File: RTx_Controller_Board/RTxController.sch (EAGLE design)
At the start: 214 parts, among them IC1 LTC4263, IC2 TLK110", SW1 COM08720, U1 STM32F407ZXT, U2 TPD4S012, X4 MINI-USB-32005-301, X8 0826-1X1T-GJ-F

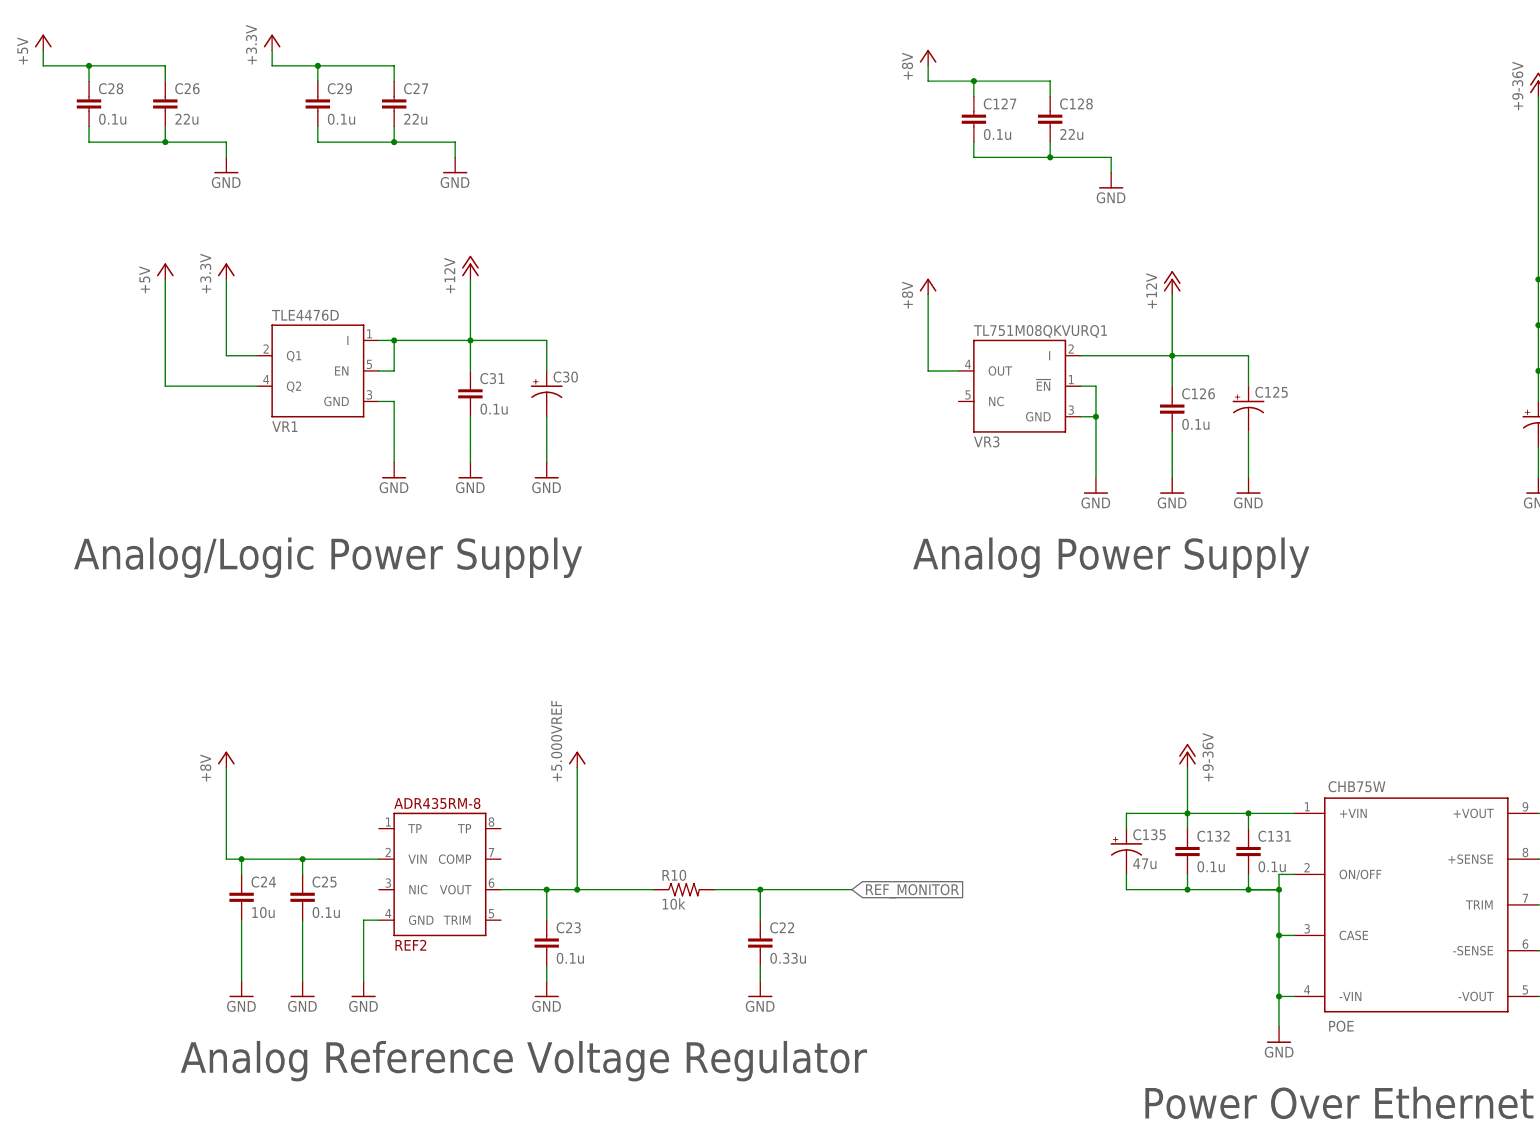
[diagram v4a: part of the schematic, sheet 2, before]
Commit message: Made modifications to address issues recorded and closed.
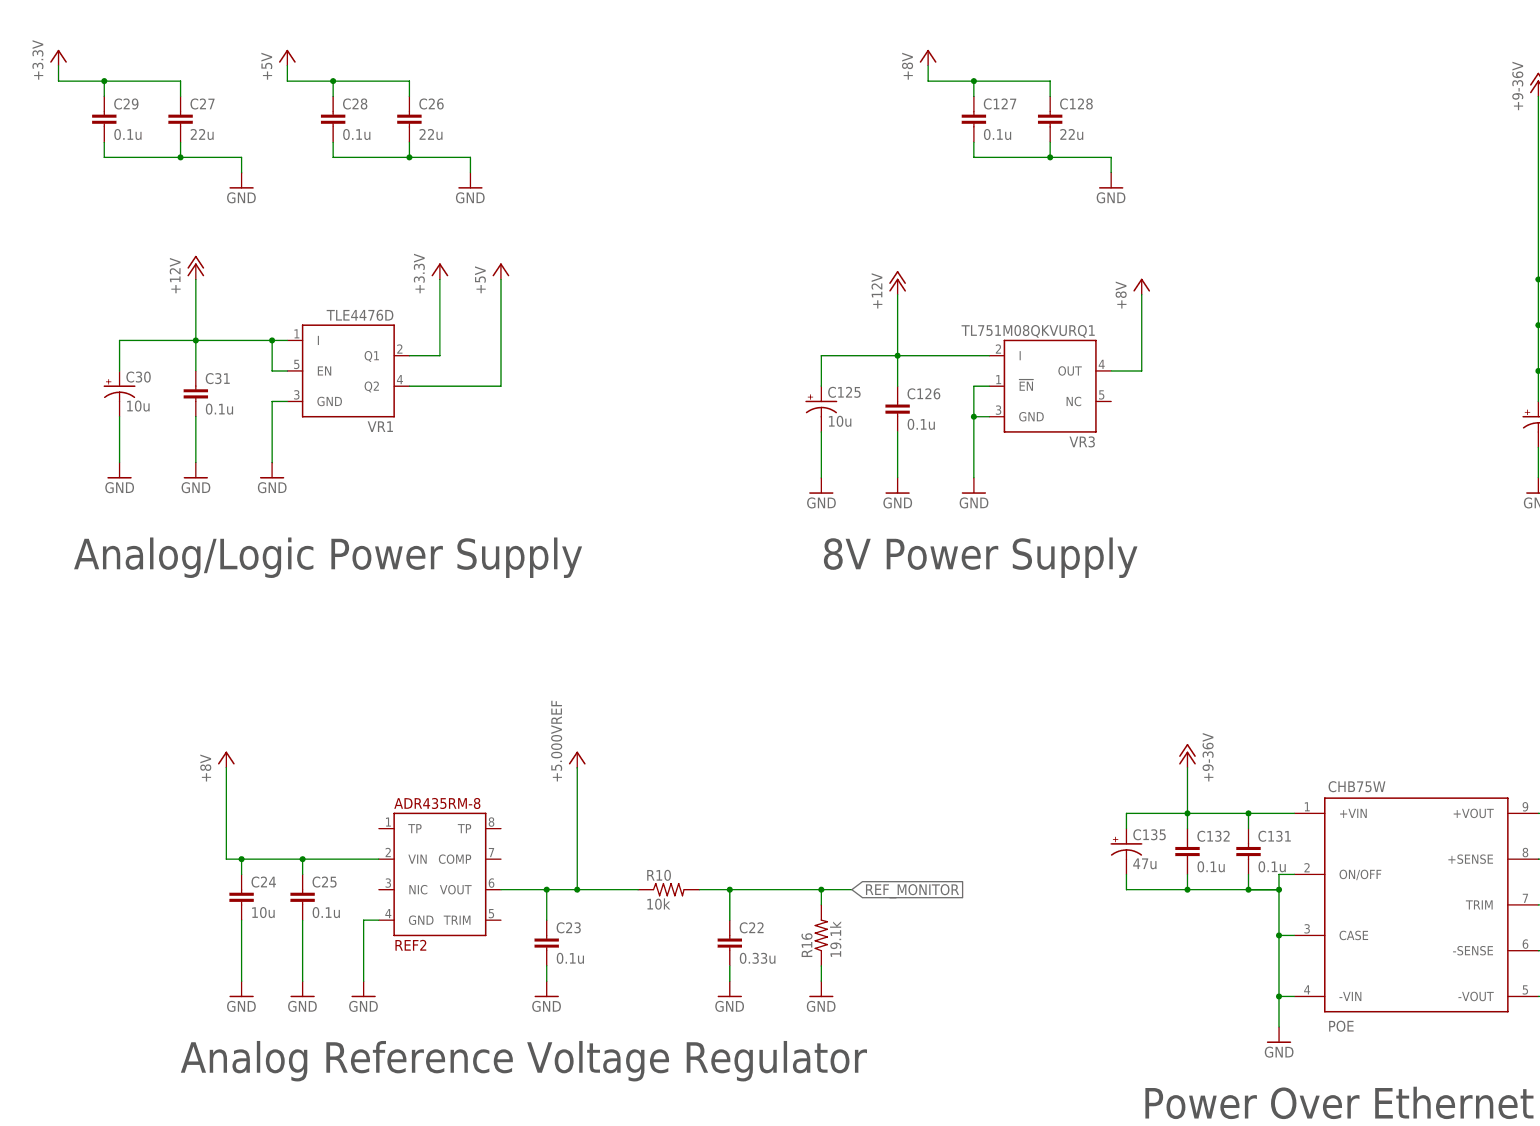
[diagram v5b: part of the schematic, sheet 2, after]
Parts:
- removed JP2: (no value), pinhead:PINHD-1X6
- removed R55, R56, R57, R58: 22, motorFeedback:R-US_R0603
- removed R59: 10k, motorFeedback:R-US_R0603
- added C55: 1u, motorFeedback:C-EUC0805
- added C72: 22u, motorFeedback:C-EUC1206
- added J22: Debug Header, headers:1.27MM_HDR_2X5
- added R16: 19.1k, motorFeedback:R-US_R0402
- added R168: 100, rcl_custom:R-US_0402-B-NOSILK
- added TP38: TPTP06R, testpad:TPTP06R
- C125, C30: value (none) -> 10u
- C92: value 0.1u -> NU
- X1: device con-subd:F09HS -> con-subd:F15HDHS
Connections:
- removed net N$30: C53.1, R23.1, R24.2
- removed net SPI_MOSI: ADC1.CNV@6, ADC1.SDI@9, ADC2.CNV@6, ADC3.CNV@6, ADC4.CNV@6, U1-IO.PB5/SPI1_MOSI@91
- removed net STM_SWCLK: R57.1, U1-IO.PA14/JTCK@76
- removed net STM_SWDIO: R56.1, U1-IO.PA13/JTMS@72
- removed net STM_SWO: R58.1, U1-IO.PB3/JTDO@89
- removed net SWD_GND1: JP2.1, R59.2
- removed net SWD_NRST: JP2.5, R55.2
- removed net SWD_SWCLK: JP2.2, R57.2
- removed net SWD_SWDIO: JP2.4, R56.2
- removed net SWD_SWO: JP2.6, R58.2
- removed net V+@8: OPAMP2-A.V+@8
- removed net VDDA: C88.1, C89.1, C90.1, C91.1, U1-PWR.VDDA@22, U1-PWR.VREF+@21
- new net ADC_CNV: U1-IO.PA4/SPI_NSS@29
- new net JTAG_TCK: J22.TCK
- new net JTAG_TDI: J22.TDI
- new net JTAG_TDO: J22.TDO
- new net JTAG_TMS: J22.TMS
- new net N$206: J22.VTREF, R168.1
- new net N$210: J22.GNDDET, TP38.TP
- new net SPI_NSS: ADC1.CNV@6, ADC1.SDI@9, ADC2.CNV@6, ADC3.CNV@6, ADC4.CNV@6
- net +3.3V: now also C53.1, C88.1, C89.1, C90.1, C91.1, R168.2, R23.1, R24.2, U1-PWR.VDDA@22, U1-PWR.VREF+@21
- net +5.000VREF: now also C55.1, C72.1, X1-12.F, X1-14.F, X1-2.F, X1-3.F; no longer X1-9.F
- net +5V: now also OPAMP2-A.V+@8
- net GND: now also C55.2, C72.2, J22.GND, J22.GND@2, R16.1, X1-5.F, X1-7.F; no longer JP2.3, R59.1, X1-2.F, X1-4.F
- net N$14: now also X1-4.F; no longer X1-3.F
- net N$6: now also X1-15.F; no longer X1-7.F
- net N$9: now also X1-11.F; no longer X1-5.F
- net NRST: now also J22.!RESET; no longer R55.1
- net REF_MONITOR: now also R16.2
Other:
- note added: "8V Power Supply"
- note added: "ADC Interrupt In"
- note added: "Debug Header"
- note added: "Ground at OpAmp"
- note added: "Place at REF pin"
- note removed: "Analog Power Supply"
- note removed: "SWD"
- moved on the sheet: C125, C126, C22, C26, C27, C28, C29, C30, C31, C44, C48, C50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

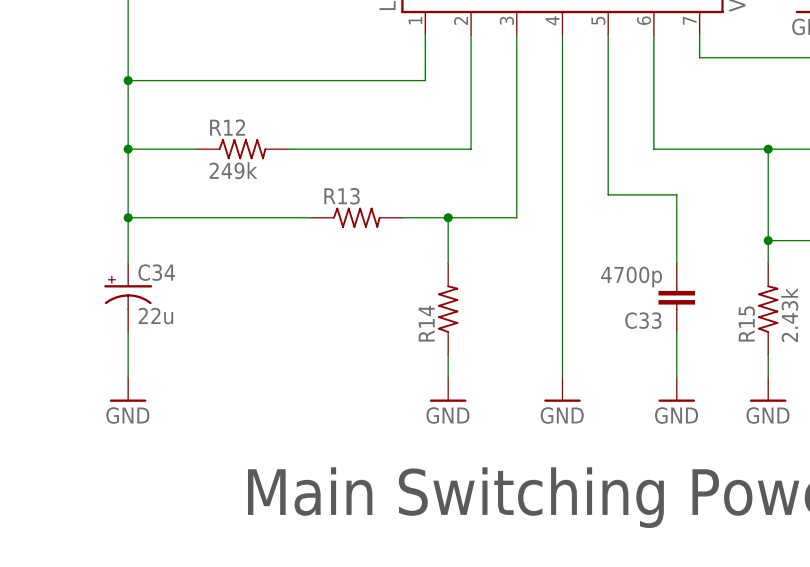
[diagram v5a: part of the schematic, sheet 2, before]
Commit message: Closed issues related to Power page of schematic.
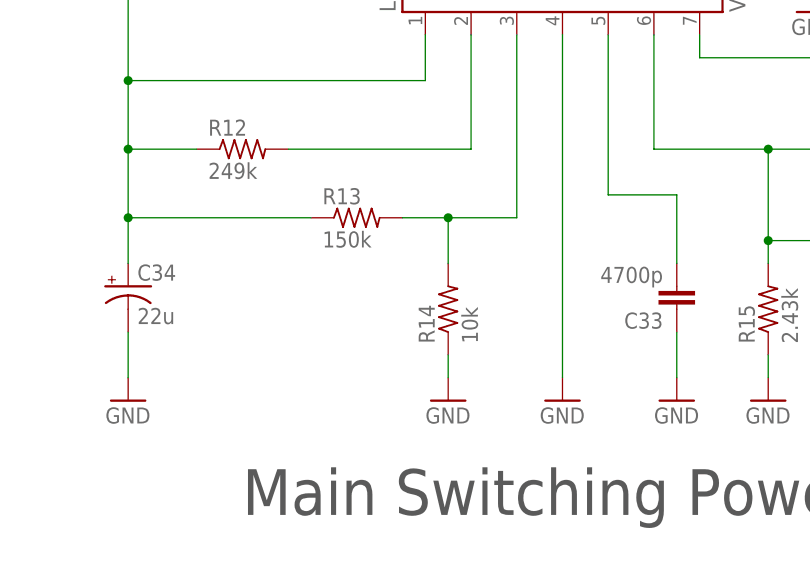
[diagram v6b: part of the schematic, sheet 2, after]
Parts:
- R13: value (none) -> 150k
- R14: value (none) -> 10k
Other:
- note added: "Add 8mil spark gaps to each signal near connector"
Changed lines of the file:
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@@
 <part name="P+19" library="motorFeedback" deviceset="+12V" device=""/>
 <part name="R12" library="motorFeedback" deviceset="R-US_" device="R0603" value="249k"/>
-<part name="R13" library="motorFeedback" deviceset="R-US_" device="R0603"/>
-<part name="R14" library="motorFeedback" deviceset="R-US_" device="R0603"/>
+<part name="R13" library="motorFeedback" deviceset="R-US_" device="R0603" value="150k"/>
+<part name="R14" library="motorFeedback" deviceset="R-US_" device="R0603" value="10k"/>
 <part name="R15" library="motorFeedback" deviceset="R-US_" device="R0603" value="2.43k"/>
 <part name="C32" library="motorFeedback" deviceset="C-EU" device="C0402" value="0.022u"/>
@@
 <text x="187.706" y="110.998" size="1.27" layer="97" rot="R180">Place at REF pin</text>
 <text x="187.706" y="52.578" size="1.27" layer="97" rot="R180">Place at REF pin</text>
+<text x="10.16" y="137.16" size="1.27" layer="97" rot="R90">Add 8mil spark gaps to each signal near connector</text>
 </plain>
 <instances>
@@
 <wire x1="398.78" y1="76.2" x2="398.78" y2="129.54" width="0.1524" layer="97" style="shortdash"/>
 <wire x1="398.78" y1="129.54" x2="332.74" y2="129.54" width="0.1524" layer="97" style="shortdash"/>
+<text x="10.16" y="25.4" size="1.27" layer="97" rot="R90">Add 8mil spark gaps to each signal near connector</text>
+<text x="10.16" y="83.82" size="1.27" layer="97" rot="R90">Add 8mil spark gaps to each signal near connector</text>
 </plain>
 <instances>

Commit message: Cleaned up schematic, began layout of RTx Controller PCB.
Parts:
- removed REF2: ADR435RM-8, motorFeedback:ADR435RM-8
- added REF1: ADR435RM-8, motorFeedback:ADR435RM-8
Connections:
- net +5.000VREF: now also REF1.VOUT@6; no longer REF2.VOUT@6
- net +8V: now also REF1.VIN@2; no longer REF2.VIN@2
- net GND: now also REF1.GND@4; no longer REF2.GND@4
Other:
- note added: "Ref Voltage Monitor Filter"
- moved on the sheet: C129, C130, C131, C132, C133, C135, C22, C23, C24, C25, C32, C33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

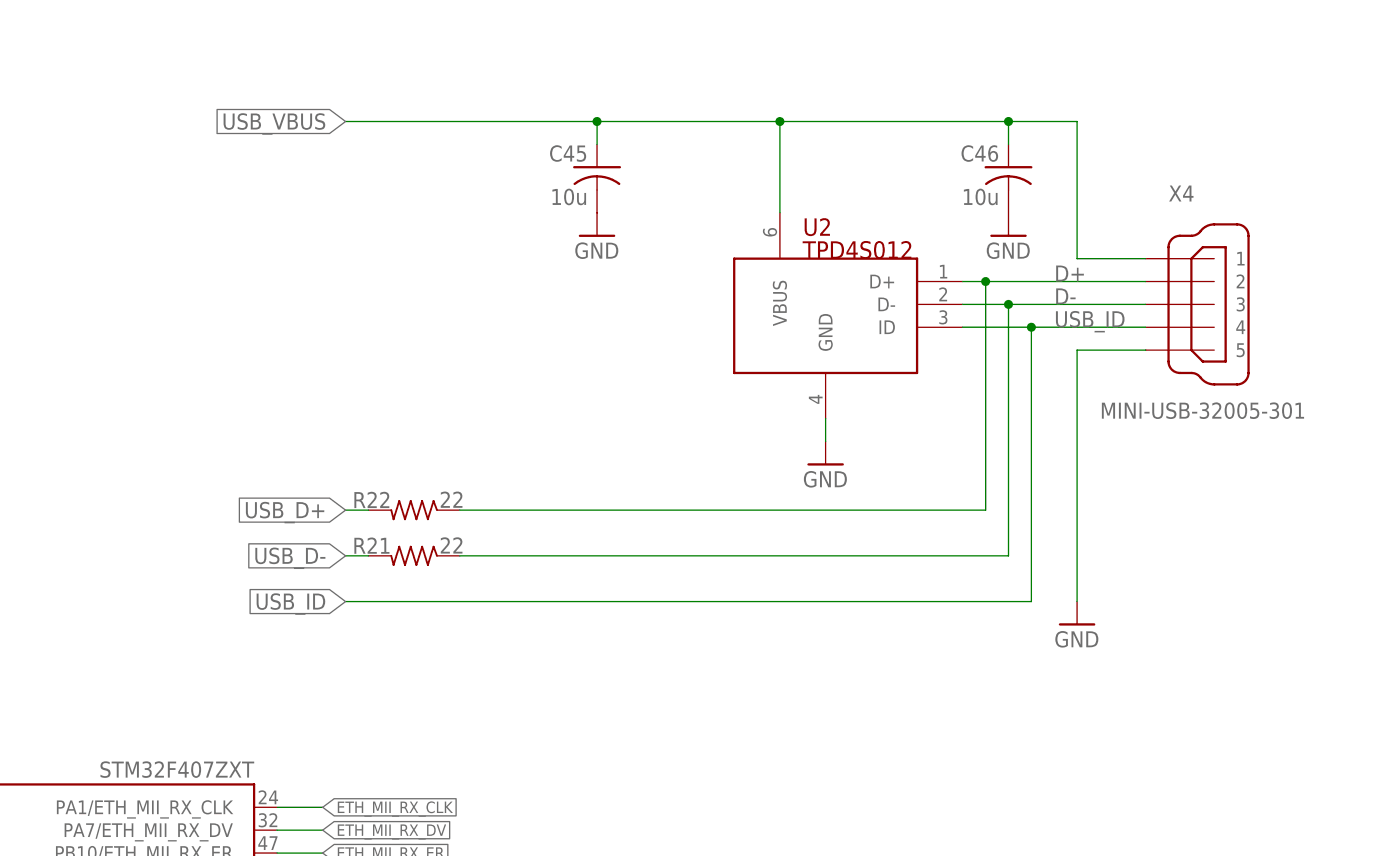
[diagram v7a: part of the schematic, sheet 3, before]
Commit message: Updated FMEA. Updated USB on schematic to include border. Updated documentation on USB.
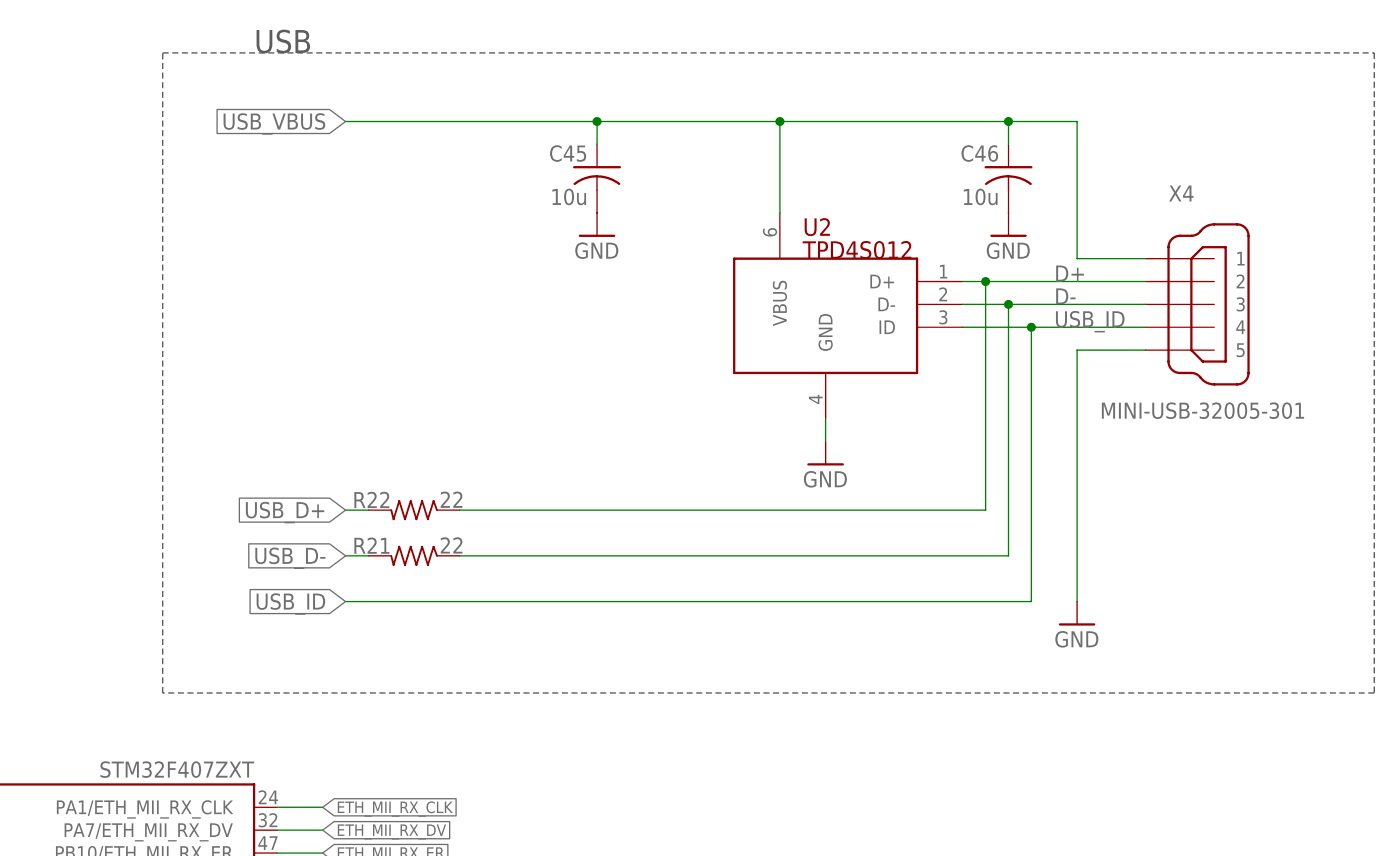
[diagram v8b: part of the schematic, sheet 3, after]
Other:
- note added: "USB"
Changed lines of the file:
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@@
 <text x="10.16" y="25.4" size="1.27" layer="97" rot="R90">Add 8mil spark gaps to each signal near connector</text>
 <text x="10.16" y="83.82" size="1.27" layer="97" rot="R90">Add 8mil spark gaps to each signal near connector</text>
+<wire x1="271.78" y1="243.84" x2="406.4" y2="243.84" width="0.1524" layer="97" style="shortdash"/>
+<wire x1="406.4" y1="243.84" x2="406.4" y2="172.72" width="0.1524" layer="97" style="shortdash"/>
+<wire x1="406.4" y1="172.72" x2="271.78" y2="172.72" width="0.1524" layer="97" style="shortdash"/>
+<wire x1="271.78" y1="172.72" x2="271.78" y2="243.84" width="0.1524" layer="97" style="shortdash"/>
+<text x="281.94" y="243.84" size="2.54" layer="97">USB</text>
 </plain>
 <instances>
